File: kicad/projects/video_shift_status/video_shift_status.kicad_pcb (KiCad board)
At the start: 2 copper layers, 203.2 x 97.8 mm, 52 parts, among them J1 peripheral_addr_bus_connector, J2 peripheral_aux_connector, J3 peripheral_membank_connector, J4 Conn_01x16_Socket, J5 Conn_01x16_Socket, J6 video_aux, J7 Conn_01x03_Pin, J8 Conn_01x04_Socket, J9 Conn_02x06_Odd_Even, U1 74HC245, U10 74HC377, U11 74HC138, U12 74HC04, U13 74HC10, U14 74HC04, U15 74HC08, U2 74HC245, U3 74HC245, U4 74HC245, U5 74HC245, U6 74HC245, U7 74HC245, U8 74HC245, U9 74HC245

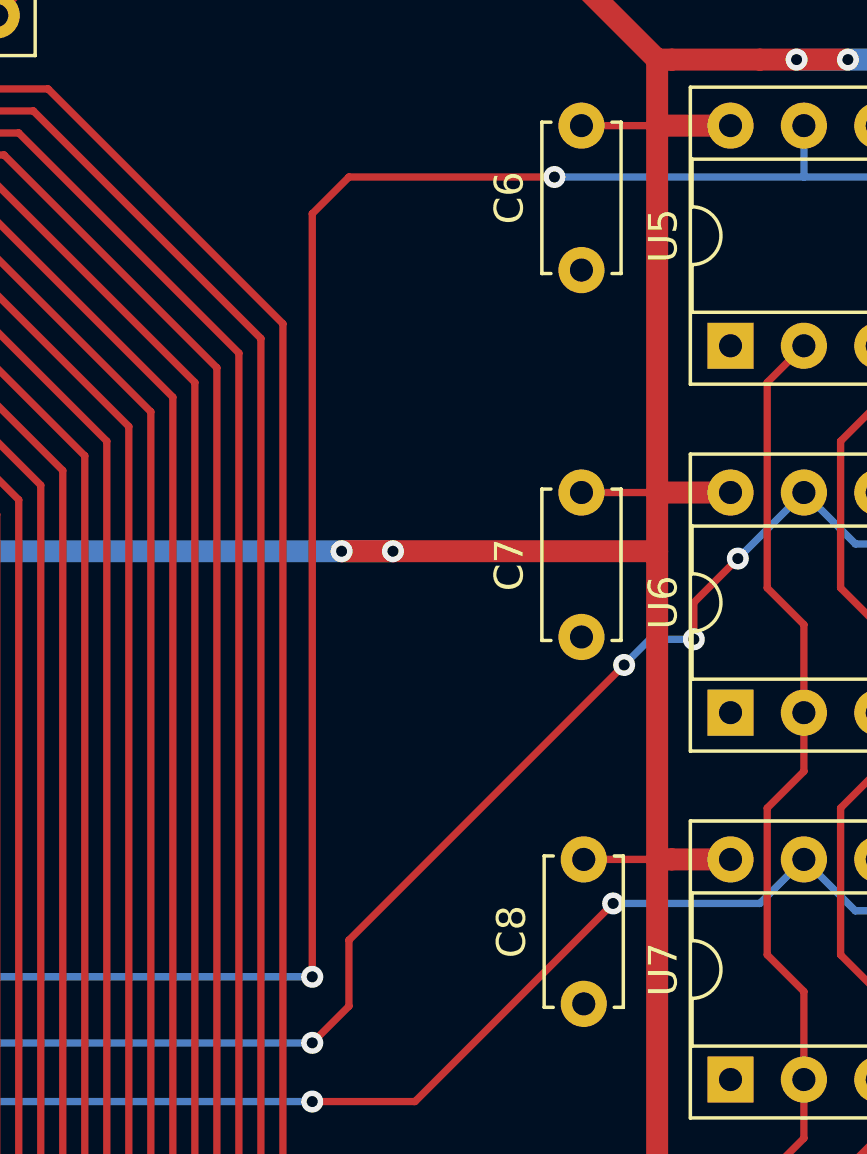
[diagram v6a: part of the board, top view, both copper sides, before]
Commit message: Row and column order made consistent on top connectors. Bank Sel cursor tech checked.
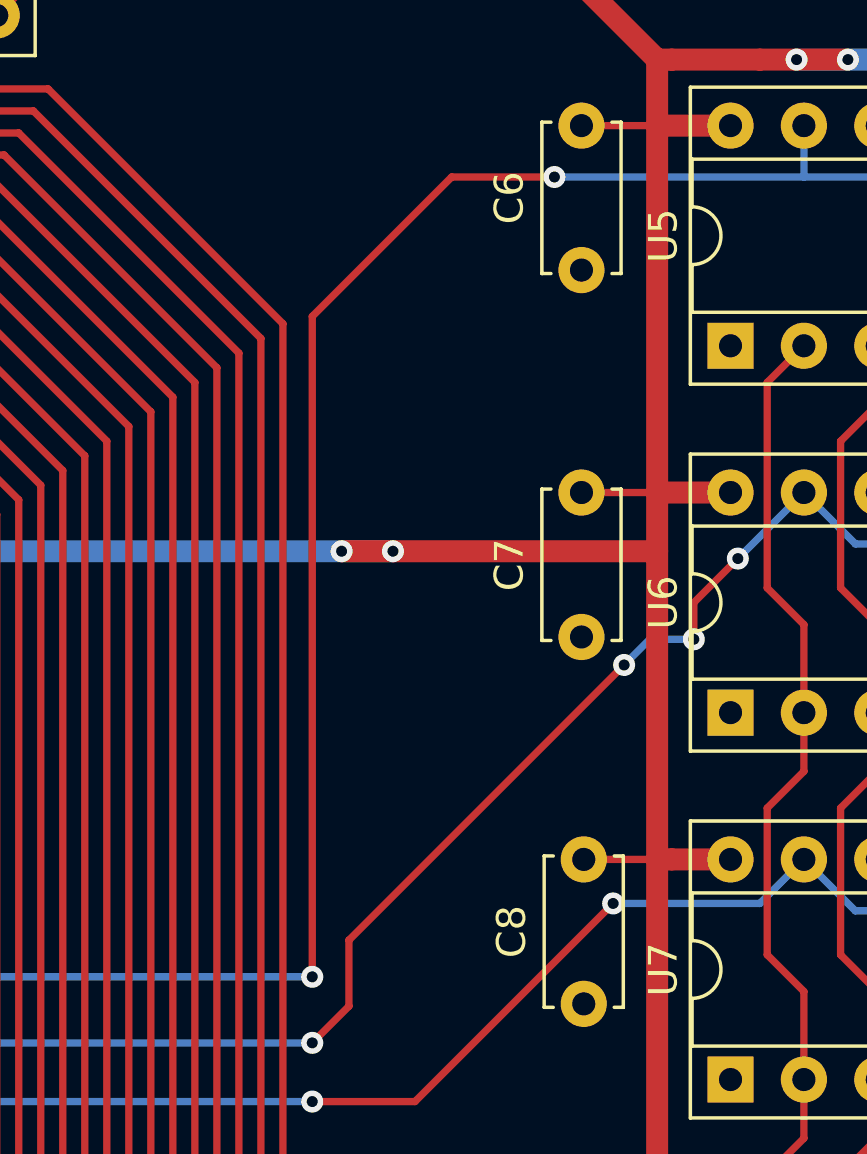
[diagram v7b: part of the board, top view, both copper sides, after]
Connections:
- J4 pad 1: /ROW_OUT_0 -> /COL_OUT_0
- J4 pad 10: /COL_OUT_1 -> /ROW_OUT_1
- J4 pad 11: /COL_OUT_2 -> /ROW_OUT_2
- J4 pad 12: /COL_OUT_3 -> /ROW_OUT_3
- J4 pad 13: /COL_OUT_4 -> /ROW_OUT_4
- J4 pad 14: /COL_OUT_5 -> /ROW_OUT_5
- J4 pad 15: /COL_OUT_6 -> /ROW_OUT_6
- J4 pad 16: /COL_OUT_7 -> /ROW_OUT_7
- J4 pad 2: /ROW_OUT_1 -> /COL_OUT_1
- J4 pad 3: /ROW_OUT_2 -> /COL_OUT_2
- J4 pad 4: /ROW_OUT_3 -> /COL_OUT_3
- J4 pad 5: /ROW_OUT_4 -> /COL_OUT_4
- J4 pad 6: /ROW_OUT_5 -> /COL_OUT_5
- J4 pad 7: /ROW_OUT_6 -> /COL_OUT_6
- J4 pad 8: /ROW_OUT_7 -> /COL_OUT_7
- J4 pad 9: /COL_OUT_0 -> /ROW_OUT_0
- J5 pad 1: /ROW_IN_0 -> /COL_IN_0
- J5 pad 10: /COL_IN_1 -> /ROW_IN_1
- J5 pad 11: /COL_IN_2 -> /ROW_IN_2
- J5 pad 12: /COL_IN_3 -> /ROW_IN_3
- J5 pad 13: /COL_IN_4 -> /ROW_IN_4
- J5 pad 14: /COL_IN_5 -> /ROW_IN_5
- J5 pad 15: /COL_IN_6 -> /ROW_IN_6
- J5 pad 16: /COL_IN_7 -> /ROW_IN_7
- J5 pad 2: /ROW_IN_1 -> /COL_IN_1
- J5 pad 3: /ROW_IN_2 -> /COL_IN_2
- J5 pad 4: /ROW_IN_3 -> /COL_IN_3
- J5 pad 5: /ROW_IN_4 -> /COL_IN_4
- J5 pad 6: /ROW_IN_5 -> /COL_IN_5
- J5 pad 7: /ROW_IN_6 -> /COL_IN_6
- J5 pad 8: /ROW_IN_7 -> /COL_IN_7
- J5 pad 9: /COL_IN_0 -> /ROW_IN_0
- U1 pad 11: /ROW_IN_0 -> /COL_IN_0
- U1 pad 12: /ROW_IN_1 -> /COL_IN_1
- U1 pad 13: /ROW_IN_2 -> /COL_IN_2
- U1 pad 14: /ROW_IN_3 -> /COL_IN_3
- U1 pad 15: /ROW_IN_4 -> /COL_IN_4
- U1 pad 16: /ROW_IN_5 -> /COL_IN_5
- U1 pad 17: /ROW_IN_6 -> /COL_IN_6
- U1 pad 18: /ROW_IN_7 -> /COL_IN_7
- U1 pad 2: /ROW_OUT_7 -> /COL_OUT_7
- U1 pad 3: /ROW_OUT_6 -> /COL_OUT_6
- U1 pad 4: /ROW_OUT_5 -> /COL_OUT_5
- U1 pad 5: /ROW_OUT_4 -> /COL_OUT_4
- U1 pad 6: /ROW_OUT_3 -> /COL_OUT_3
- U1 pad 7: /ROW_OUT_2 -> /COL_OUT_2
- U1 pad 8: /ROW_OUT_1 -> /COL_OUT_1
- U1 pad 9: /ROW_OUT_0 -> /COL_OUT_0
- U2 pad 11: /ROW_IN_1 -> /COL_IN_1
- U2 pad 12: /ROW_IN_2 -> /COL_IN_2
- U2 pad 13: /ROW_IN_3 -> /COL_IN_3
- U2 pad 14: /ROW_IN_4 -> /COL_IN_4
- U2 pad 15: /ROW_IN_5 -> /COL_IN_5
- U2 pad 16: /ROW_IN_6 -> /COL_IN_6
- U2 pad 17: /ROW_IN_7 -> /COL_IN_7
- U2 pad 2: /ROW_OUT_7 -> /COL_OUT_7
- U2 pad 3: /ROW_OUT_6 -> /COL_OUT_6
- U2 pad 4: /ROW_OUT_5 -> /COL_OUT_5
- U2 pad 5: /ROW_OUT_4 -> /COL_OUT_4
- U2 pad 6: /ROW_OUT_3 -> /COL_OUT_3
- U2 pad 7: /ROW_OUT_2 -> /COL_OUT_2
- U2 pad 8: /ROW_OUT_1 -> /COL_OUT_1
- U2 pad 9: /ROW_OUT_0 -> /COL_OUT_0
- U3 pad 11: /ROW_IN_2 -> /COL_IN_2
- U3 pad 12: /ROW_IN_3 -> /COL_IN_3
- U3 pad 13: /ROW_IN_4 -> /COL_IN_4
- U3 pad 14: /ROW_IN_5 -> /COL_IN_5
- U3 pad 15: /ROW_IN_6 -> /COL_IN_6
- U3 pad 16: /ROW_IN_7 -> /COL_IN_7
- U3 pad 2: /ROW_OUT_7 -> /COL_OUT_7
- U3 pad 3: /ROW_OUT_6 -> /COL_OUT_6
- U3 pad 4: /ROW_OUT_5 -> /COL_OUT_5
- U3 pad 5: /ROW_OUT_4 -> /COL_OUT_4
- U3 pad 6: /ROW_OUT_3 -> /COL_OUT_3
- U3 pad 7: /ROW_OUT_2 -> /COL_OUT_2
- U3 pad 8: /ROW_OUT_1 -> /COL_OUT_1
- U3 pad 9: /ROW_OUT_0 -> /COL_OUT_0
- U4 pad 11: /ROW_IN_3 -> /COL_IN_3
- U4 pad 12: /ROW_IN_4 -> /COL_IN_4
- U4 pad 13: /ROW_IN_5 -> /COL_IN_5
- U4 pad 14: /ROW_IN_6 -> /COL_IN_6
- U4 pad 15: /ROW_IN_7 -> /COL_IN_7
- U4 pad 2: /ROW_OUT_7 -> /COL_OUT_7
- U4 pad 3: /ROW_OUT_6 -> /COL_OUT_6
- U4 pad 4: /ROW_OUT_5 -> /COL_OUT_5
- U4 pad 5: /ROW_OUT_4 -> /COL_OUT_4
- U4 pad 6: /ROW_OUT_3 -> /COL_OUT_3
- U4 pad 7: /ROW_OUT_2 -> /COL_OUT_2
- U4 pad 8: /ROW_OUT_1 -> /COL_OUT_1
- U4 pad 9: /ROW_OUT_0 -> /COL_OUT_0
- U5 pad 11: /COL_IN_0 -> /ROW_IN_0
- U5 pad 12: /COL_IN_1 -> /ROW_IN_1
- U5 pad 13: /COL_IN_2 -> /ROW_IN_2
- U5 pad 14: /COL_IN_3 -> /ROW_IN_3
- U5 pad 15: /COL_IN_4 -> /ROW_IN_4
- U5 pad 16: /COL_IN_5 -> /ROW_IN_5
- U5 pad 17: /COL_IN_6 -> /ROW_IN_6
- U5 pad 18: /COL_IN_7 -> /ROW_IN_7
- U5 pad 2: /COL_OUT_7 -> /ROW_OUT_7
- U5 pad 3: /COL_OUT_6 -> /ROW_OUT_6
- U5 pad 4: /COL_OUT_5 -> /ROW_OUT_5
- U5 pad 5: /COL_OUT_4 -> /ROW_OUT_4
- U5 pad 6: /COL_OUT_3 -> /ROW_OUT_3
- U5 pad 7: /COL_OUT_2 -> /ROW_OUT_2
- U5 pad 8: /COL_OUT_1 -> /ROW_OUT_1
- U5 pad 9: /COL_OUT_0 -> /ROW_OUT_0
- U6 pad 11: /COL_IN_1 -> /ROW_IN_1
- U6 pad 12: /COL_IN_2 -> /ROW_IN_2
- U6 pad 13: /COL_IN_3 -> /ROW_IN_3
- U6 pad 14: /COL_IN_4 -> /ROW_IN_4
- U6 pad 15: /COL_IN_5 -> /ROW_IN_5
- U6 pad 16: /COL_IN_6 -> /ROW_IN_6
- U6 pad 17: /COL_IN_7 -> /ROW_IN_7
- U6 pad 2: /COL_OUT_7 -> /ROW_OUT_7
- U6 pad 3: /COL_OUT_6 -> /ROW_OUT_6
- U6 pad 4: /COL_OUT_5 -> /ROW_OUT_5
- U6 pad 5: /COL_OUT_4 -> /ROW_OUT_4
- U6 pad 6: /COL_OUT_3 -> /ROW_OUT_3
- U6 pad 7: /COL_OUT_2 -> /ROW_OUT_2
- U6 pad 8: /COL_OUT_1 -> /ROW_OUT_1
- U6 pad 9: /COL_OUT_0 -> /ROW_OUT_0
- U7 pad 11: /COL_IN_2 -> /ROW_IN_2
- U7 pad 12: /COL_IN_3 -> /ROW_IN_3
- U7 pad 13: /COL_IN_4 -> /ROW_IN_4
- U7 pad 14: /COL_IN_5 -> /ROW_IN_5
- U7 pad 15: /COL_IN_6 -> /ROW_IN_6
- U7 pad 16: /COL_IN_7 -> /ROW_IN_7
- U7 pad 2: /COL_OUT_7 -> /ROW_OUT_7
- U7 pad 3: /COL_OUT_6 -> /ROW_OUT_6
- U7 pad 4: /COL_OUT_5 -> /ROW_OUT_5
- U7 pad 5: /COL_OUT_4 -> /ROW_OUT_4
- U7 pad 6: /COL_OUT_3 -> /ROW_OUT_3
- U7 pad 7: /COL_OUT_2 -> /ROW_OUT_2
- U7 pad 8: /COL_OUT_1 -> /ROW_OUT_1
- U7 pad 9: /COL_OUT_0 -> /ROW_OUT_0
- U8 pad 11: /COL_IN_3 -> /ROW_IN_3
- U8 pad 12: /COL_IN_4 -> /ROW_IN_4
- U8 pad 13: /COL_IN_5 -> /ROW_IN_5
- U8 pad 14: /COL_IN_6 -> /ROW_IN_6
- U8 pad 15: /COL_IN_7 -> /ROW_IN_7
- U8 pad 2: /COL_OUT_7 -> /ROW_OUT_7
- U8 pad 3: /COL_OUT_6 -> /ROW_OUT_6
- U8 pad 4: /COL_OUT_5 -> /ROW_OUT_5
- U8 pad 5: /COL_OUT_4 -> /ROW_OUT_4
- U8 pad 6: /COL_OUT_3 -> /ROW_OUT_3
- U8 pad 7: /COL_OUT_2 -> /ROW_OUT_2
- U8 pad 8: /COL_OUT_1 -> /ROW_OUT_1
- U8 pad 9: /COL_OUT_0 -> /ROW_OUT_0
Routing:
- net /ROW_OUT_7: track 209.2 -> 181.6 mm, vias 2 -> 0
- net /COL_OUT_7: track 181.6 -> 209.2 mm, vias 0 -> 2
- net /ROW_OUT_5: track 211.3 -> 184.9 mm
- net /ROW_OUT_2: track 214.5 -> 188.1 mm
- net /COL_OUT_5: track 184.9 -> 211.3 mm
- net /COL_OUT_2: track 188.1 -> 214.5 mm
- net /ROW_OUT_3: track 213.5 -> 187.1 mm
- net /ROW_OUT_1: track 215.6 -> 189.2 mm
- net /COL_OUT_3: track 187.1 -> 213.5 mm
- net /COL_OUT_1: track 189.2 -> 215.6 mm
- net /ROW_OUT_6: track 210.2 -> 183.8 mm
- net /COL_OUT_6: track 183.8 -> 210.2 mm
- net /ROW_OUT_0: track 216.7 -> 190.3 mm
- net /COL_OUT_0: track 190.3 -> 216.7 mm
- net /ROW_OUT_4: track 212.4 -> 186.0 mm
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
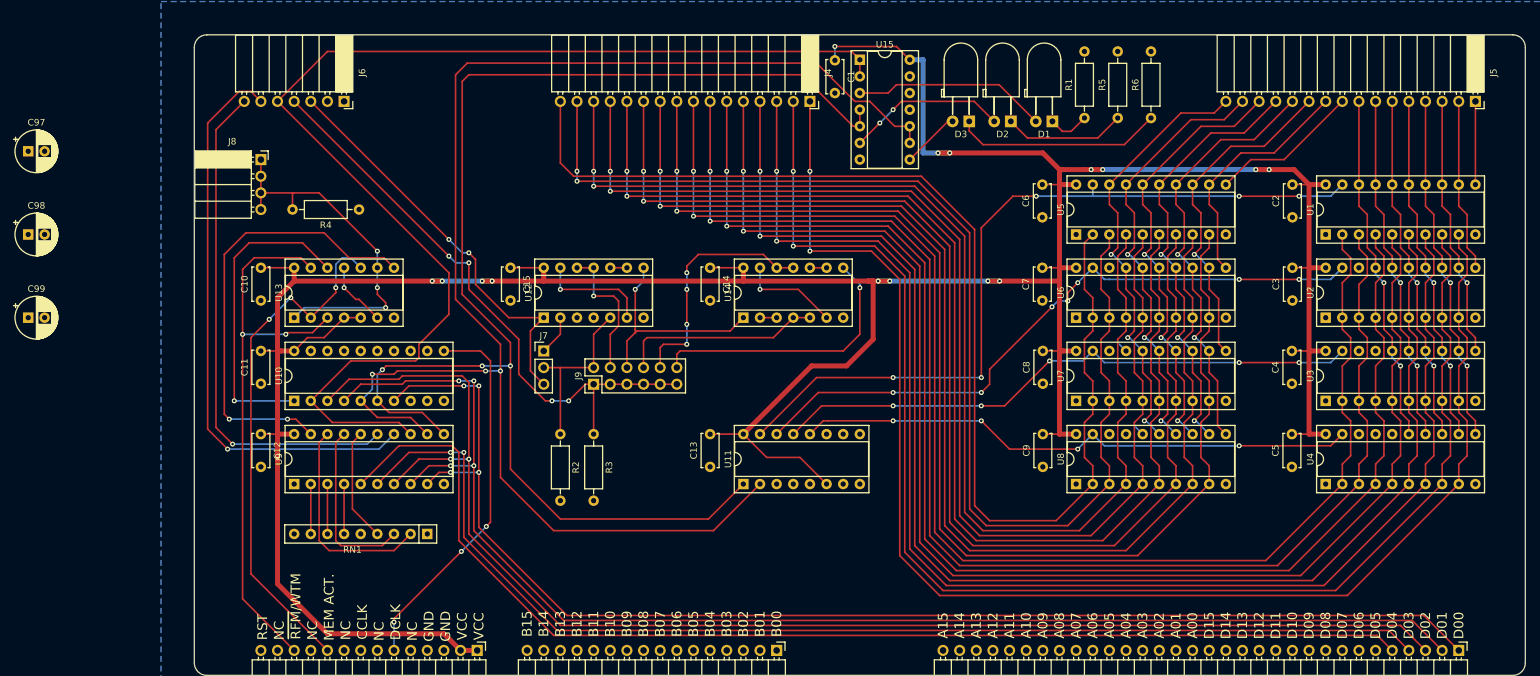
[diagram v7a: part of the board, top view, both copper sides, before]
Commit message: Prep video out for RGB shuffle. Some work on shift status for tech checks, not complete yet.
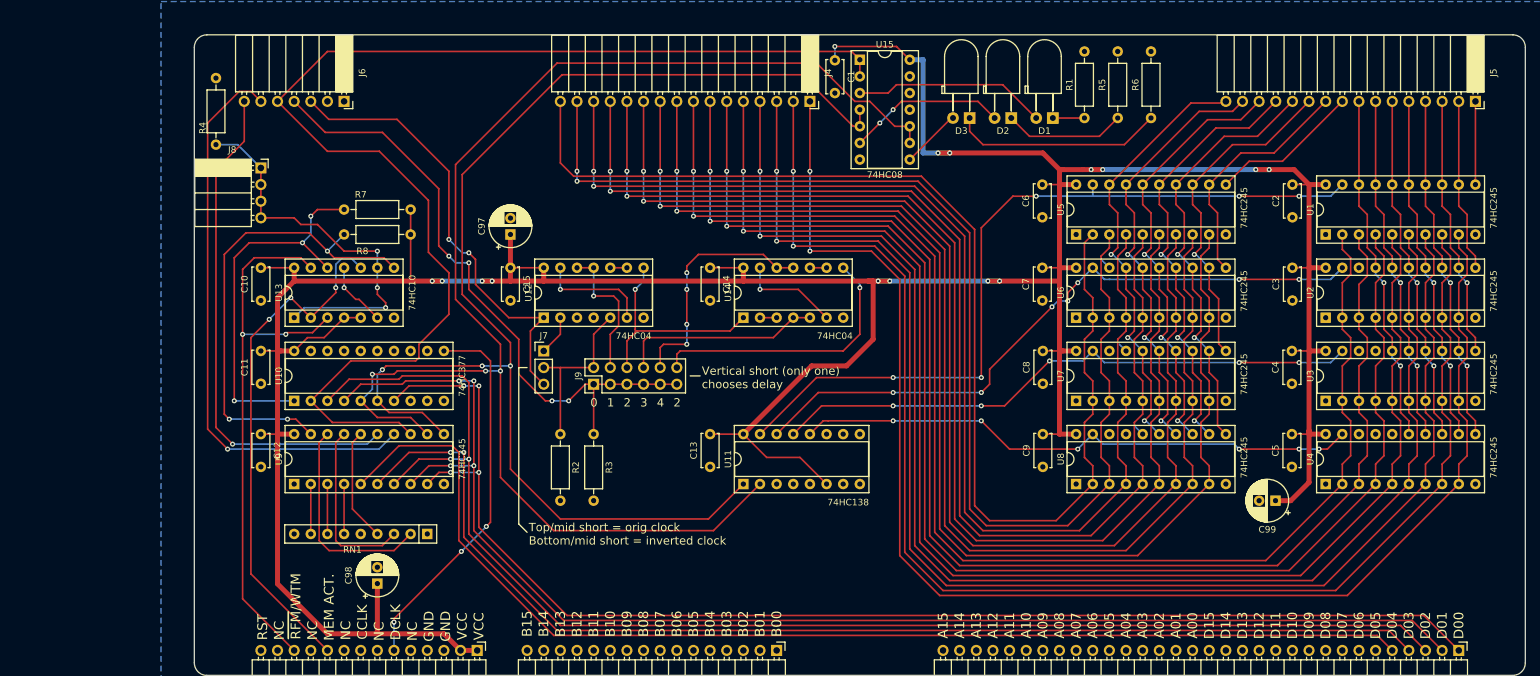
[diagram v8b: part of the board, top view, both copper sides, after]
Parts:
- added R7: 10K, Resistor_THT:R_Axial_DIN0207_L6.3mm_D2.5mm_P10.16mm_Horizontal, F.Cu at (83.8, 77.5)
- added R8: 10K, Resistor_THT:R_Axial_DIN0207_L6.3mm_D2.5mm_P10.16mm_Horizontal, F.Cu at (73.7, 81.3)
- moved C99 192.5 mm to (215.9, 121.9), turned to 180 degrees
- moved C98 75.4 mm to (78.7, 134.6), turned to 90 degrees
- moved C97 74.7 mm to (99.1, 81.3), turned to 90 degrees
- moved R4 29.7 mm to (54.1, 57.4), turned to -90 degrees
- moved J8 1.27 mm to (61.0, 71.1)
- moved D1 0.52 mm to (181.9, 63.5)
- moved D2 0.52 mm to (175.5, 63.5)
- moved D3 0.52 mm to (169.2, 63.5)
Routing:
- net VCC: track 523.2 -> 563.5 mm
- net /~{WRITE}: track 47.7 -> 57.8 mm, vias 1 -> 3
- net /SHIFT_SEL_0: track 207.2 -> 198.9 mm
- net /SHIFT_SEL_1: track 223.7 -> 215.7 mm
- net /PIX_CLK_RAW: track 63.3 -> 69.4 mm
- net /PIX_CLK_MOD: track 91.5 -> 96.7 mm
- net /BANK_SEL: track 183.6 -> 188.2 mm
- net /ADDRESSED: track 55.4 -> 59.6 mm
- net /~{READ}: track 68.3 -> 71.9 mm, vias 2 -> 3
- net GND: track 3.23 -> 5.03 mm
- net Net-(D1-K): track 6.36 -> 4.83 mm
- net /~{SHIFT_3}: track 86.3 -> 86.8 mm, vias 4 -> 6
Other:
- board text added: "0"
- board text added: "1"
- board text added: "2"
- board text added: "3"
- board text added: "4"
- board text added: "Top/mid short = orig clock Bottom/mid short = inverted clock"
- board text added: "Vertical short (only one) chooses delay"
